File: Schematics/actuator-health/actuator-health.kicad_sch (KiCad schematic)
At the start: 26 parts, among them J1 AFG connection, J2 PSU 5V connection, J3 Scope CH1, J4 Scope CH2, U1 MCP6022, U2 Pololu_4048_ACS724_05AU

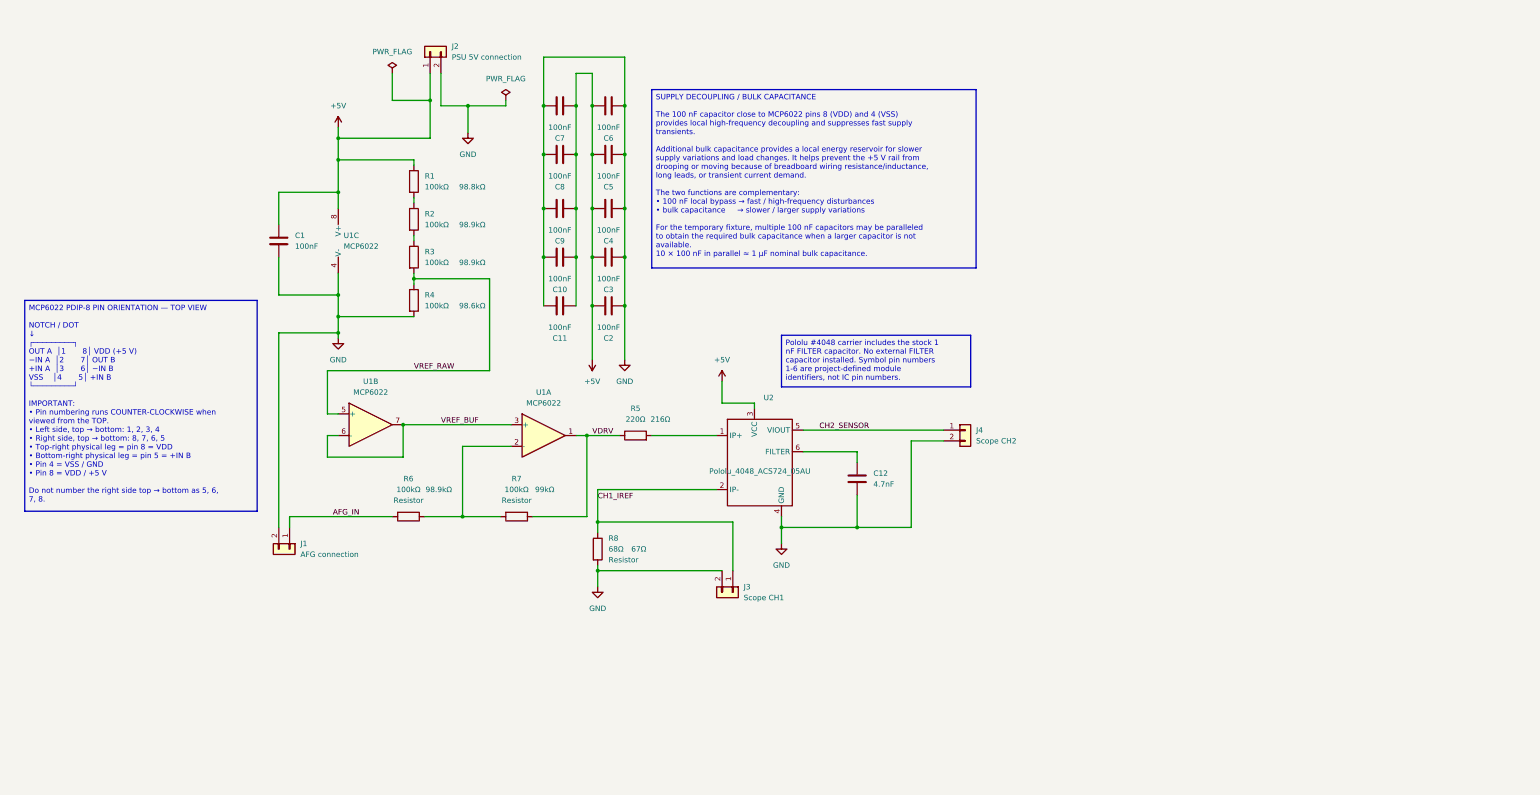
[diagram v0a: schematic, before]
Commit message: Stage B: prepare schematic for AFE bring-up
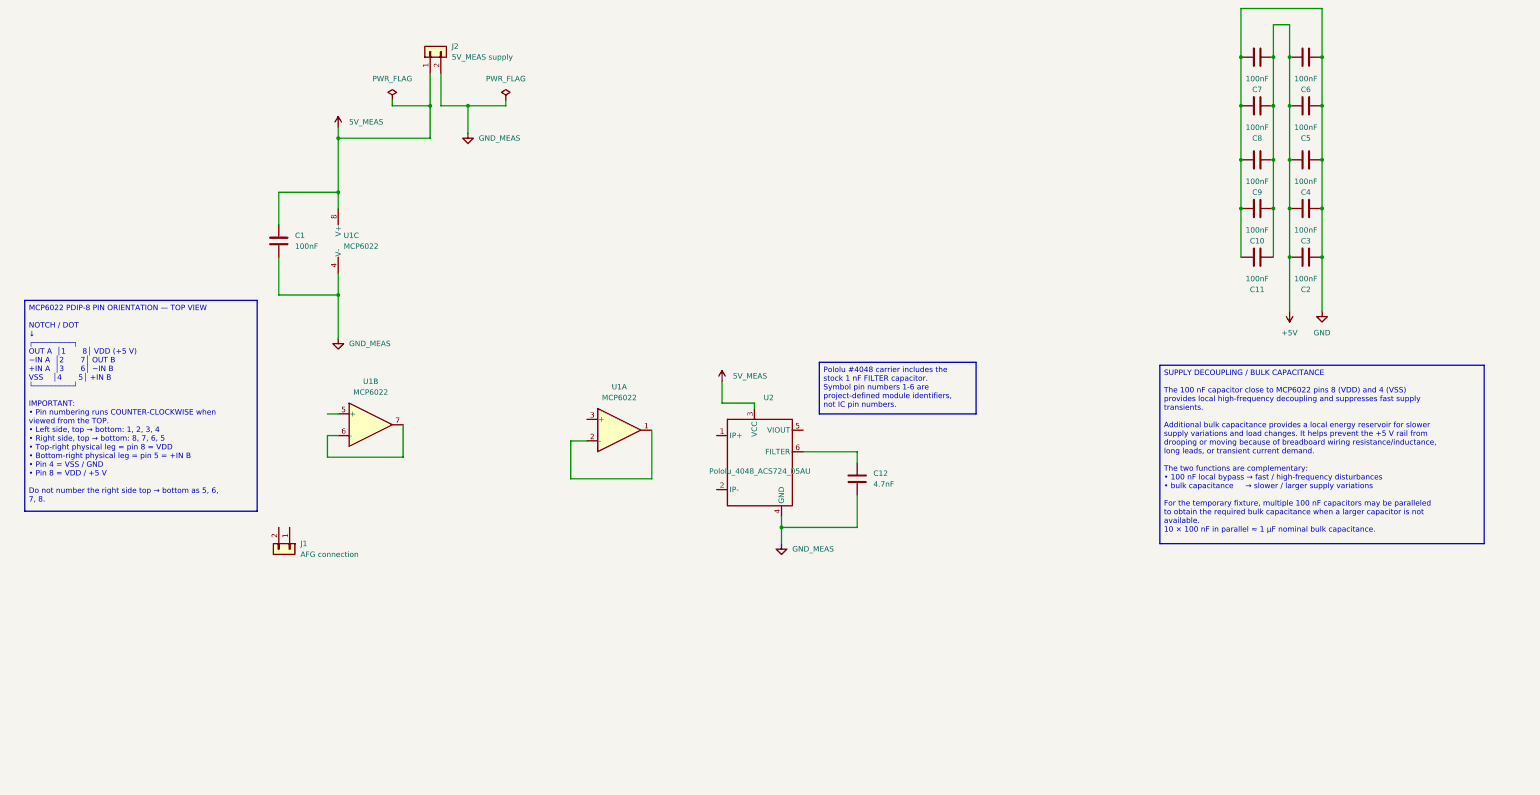
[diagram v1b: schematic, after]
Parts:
- removed J3: Scope CH1, symbol Connector_Generic:Conn_01x02
- removed J4: Scope CH2, symbol Connector_Generic:Conn_01x02
- removed R1, R2, R3, R4, R6, R7: 100kΩ, symbol Device:R
- removed R5: 220Ω, symbol Device:R
- removed R8: 68Ω, symbol Device:R
- J2: value PSU 5V connection -> 5V_MEAS supply
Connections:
- net VDRV is gone; now on an unnamed net: U1.1
- net +5V: no longer C1.1, J2.1 (Pin_1), U1.8 (V+), U2.3 (VCC)
- net GND: no longer C1.2, C12.2, J1.2 (Pin_2), J2.2 (Pin_2), U1.4 (V-), U2.4 (GND)
- net AFG_IN: no longer names the net of J1.1 (Pin_1)
- net CH1_IREF: no longer names the net of U2.2 (IP-)
- net CH2_SENSOR: no longer names the net of U2.5 (VIOUT)
- net VREF_BUF: no longer names the net of U1.6 (-), U1.7
- net VREF_BUF: no longer U1.3 (+)
- net VREF_RAW: no longer names the net of U1.5 (+)
- new net 5V_MEAS: C1.1, J2.1 (Pin_1), U1.8 (V+), U2.3 (VCC)
- new net GND_MEAS: C1.2, C12.2, J2.2 (Pin_2), U1.4 (V-), U2.4 (GND)
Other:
- moved on the sheet: C10, C11, C2, C3, C4, C5, C6, C7, C8, C9, U1A

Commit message: Stage B: implement Rev-1 AFE schematic
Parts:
- removed C10, C11, C9: 100nF, symbol Device:C
- added J3: UNO R4 A0, symbol Connector_Generic:Conn_01x01
- added R1, R2: 9.76k, symbol Device:R
- added R3, R4: 4.07k, symbol Device:R
- added R5: 1k, symbol Device:R
- added TP1: TP_5V, symbol Connector:TestPoint
- added TP2: TP_GND, symbol Connector:TestPoint
- added TP3: TP_SENSOR, symbol Connector:TestPoint
- added TP4: TP_AFE, symbol Connector:TestPoint
- C2, C5: value 100nF -> 1.0 nF
- C3: value 100nF -> 1.2 nF
- C4: value 100nF -> 6.8 nF
- C6: value 100nF -> 10 µF
- C7: value 100nF -> 100pF
- J1: value AFG connection -> AFE TEST / AFG
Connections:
- net 5V_MEAS: now also C6.1, C8.1, TP1.1
- net GND_MEAS: now also C2.1, C5.1, C6.2, C7.2, C8.2, J1.2 (Pin_2), TP2.1
- net TP_SENSOR: now reaches J1.1 (Pin_1)
- net TP_SENSOR: now also U2.5 (VIOUT), R1.1, TP3.1
- net OUTA: now reaches U1.1, U1.2 (-)
- net OUTA: now also C3.1, R3.1
- net N2A: now reaches U1.3 (+)
- net N2A: now also C2.2, R2.2
- net N2B: now reaches U1.5 (+)
- net N2B: now also C5.2, R4.2
- net TP_AFE: now reaches U1.6 (-), U1.7
- net TP_AFE: now also C4.1, R5.1, TP4.1
- removed net +5V: C2.2, C3.2, C4.2, C5.2, C6.2, C7.1, C8.1
- removed net GND: C2.1, C3.1, C4.1, C5.1, C6.1, C7.2, C8.2
- new net ADC_IN: C7.1, J3.1 (Pin_1), R5.2
- new net N1A: C3.2, R1.2, R2.1
- new net N1B: C4.2, R3.2, R4.1
- no-connect marks 0 -> 2
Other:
- moved on the sheet: C1, C12, J1, J2, U1A, U1B, U1C, U2

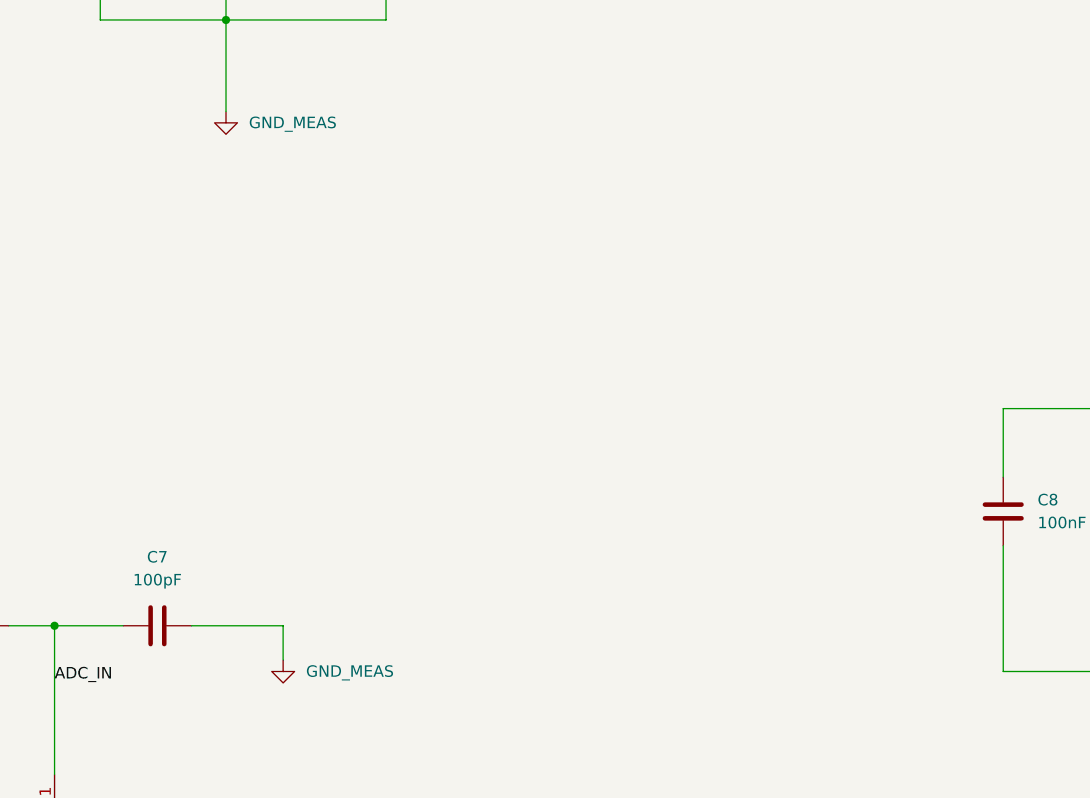
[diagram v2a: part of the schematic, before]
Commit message: Schematics merged. Unused deleted.
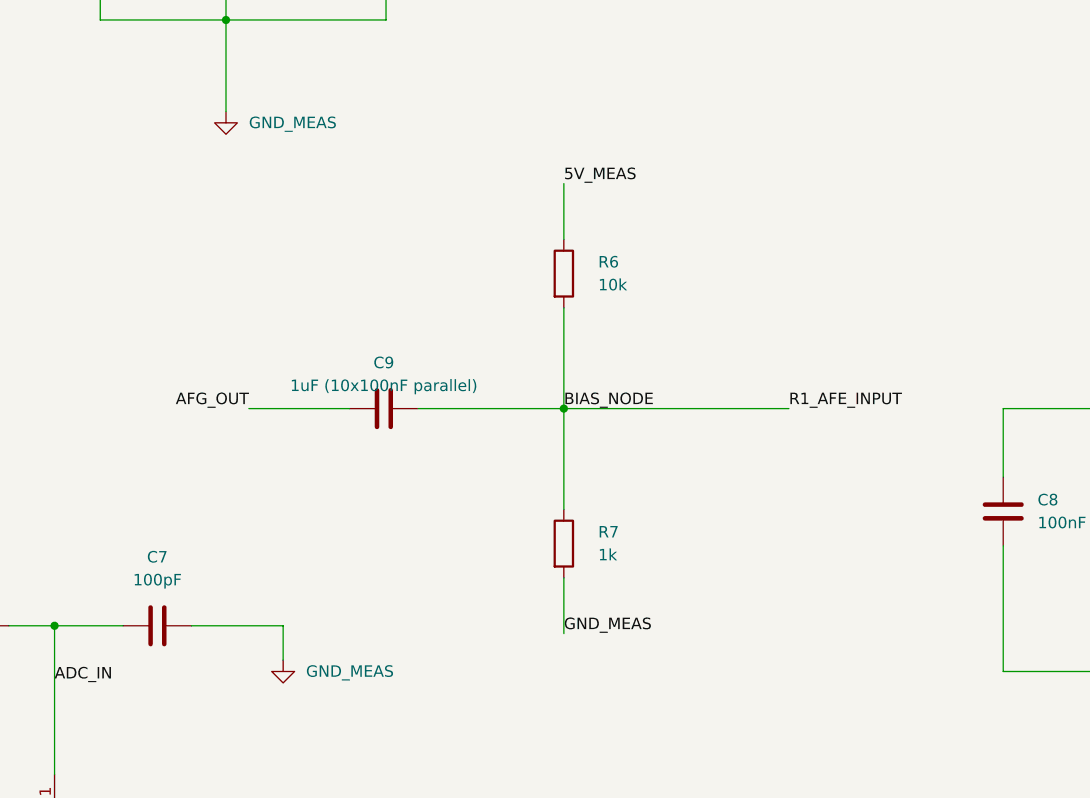
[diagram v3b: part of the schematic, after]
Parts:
- added C9: 1uF (10x100nF parallel), symbol Device:C
- added R6: 10k, symbol Device:R
- added R7: 1k, symbol Device:R
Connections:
- net 5V_MEAS: now also R6.1
- net GND_MEAS: now also R7.2
- new net AFG_OUT: C9.1
- new net BIAS_NODE: C9.2, R6.2, R7.1
